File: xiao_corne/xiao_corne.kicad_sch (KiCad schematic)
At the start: 168 parts, among them J1 Conn_01x04_Socket, J10 Conn_01x04_Socket, J2 Conn_01x04_Socket, J3 Conn_01x04_Socket, J4 Conn_01x04_Socket, J5 Conn_01x04_Socket, J6 Conn_01x04_Socket, J7 Conn_01x04_Socket, J8 Conn_01x04_Socket, J9 Conn_01x04_Socket, SW1 SW_Push, SW10 SW_Push, SW11 SW_Push, SW12 SW_Push, SW13 SW_Push, SW14 SW_Push, SW15 SW_Push, SW16 SW_Push, SW17 SW_Push, SW18 SW_Push, SW19 SW_Push, SW2 SW_Push, SW20 SW_Push, SW21 SW_Push, SW22 SW_Push, SW23 SW_Push, SW24 SW_Push, SW25 SW_Push, SW26 SW_Push, SW27 SW_Push, SW28 SW_Push, SW29 SW_Push, SW3 SW_Push, SW30 SW_Push, SW31 SW_Push, SW32 SW_Push, SW33 SW_Push, SW34 SW_Push, SW35 SW_Push, SW36 SW_Push, SW37 SW_Push, SW38 SW_Push, SW39 SW_Push, SW4 SW_Push, SW40 SW_Push, SW41 SW_Push, SW42 SW_Push, SW5 SW_Push, SW6 SW_Push, SW7 SW_Push, SW8 SW_Push, SW9 SW_Push, U1 SN74AHCT125DR, U2 SN74AHCT125DR, U3 XIAO-HALF-HOLE-23P, U4 XIAO-HALF-HOLE-23P, U5 TPS61202DRCR, U6 TPS61202DRCR

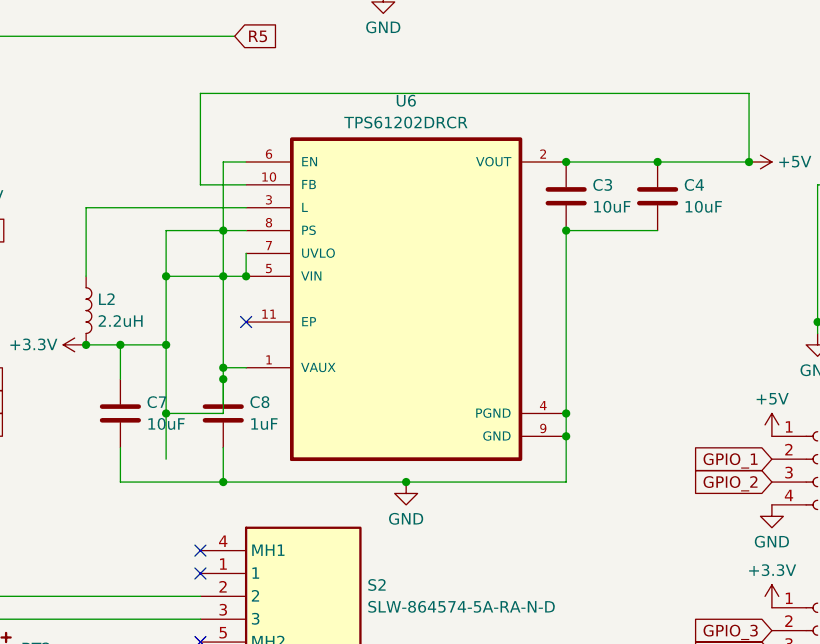
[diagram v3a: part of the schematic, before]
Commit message: Found some issues with the PCB, updated layout
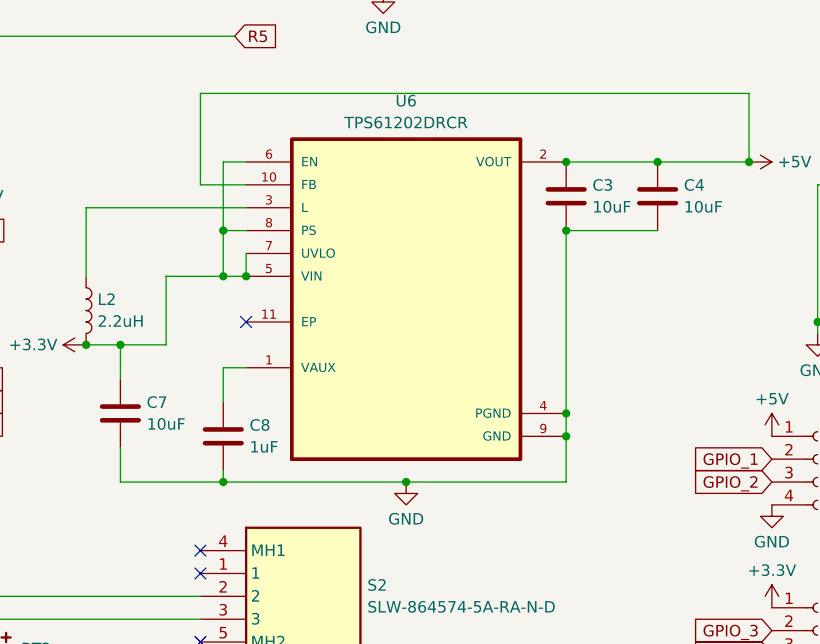
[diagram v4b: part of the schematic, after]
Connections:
- net +3.3V: no longer C8.2, U6.1 (VAUX)
- new net: C8.2, U6.1 (VAUX)
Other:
- moved on the sheet: C8
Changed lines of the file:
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@@
 	)
 	(junction
-		(at 415.29 152.4)
-		(diameter 0)
-		(color 0 0 0 0)
-	)
-	(junction
 		(at 213.36 67.31)
 		(diameter 0)
@@
 	)
 	(junction
-		(at 408.94 148.59)
-		(diameter 0)
-		(color 0 0 0 0)
-	)
-	(junction
 		(at 400.05 38.1)
 		(diameter 0)
@@
 	)
 	(junction
+		(at 453.39 128.27)
+		(diameter 0)
+		(color 0 0 0 0)
+	)
+	(junction
 		(at 116.84 38.1)
 		(diameter 0)
@@
 	)
 	(junction
-		(at 408.94 140.97)
-		(diameter 0)
-		(color 0 0 0 0)
-	)
-	(junction
 		(at 453.39 156.21)
 		(diameter 0)
@@
 	)
 	(junction
-		(at 453.39 128.27)
-		(diameter 0)
-		(color 0 0 0 0)
-	)
-	(junction
 		(at 228.6 82.55)
 		(diameter 0)
@@
 	)
 	(junction
-		(at 408.94 156.21)
-		(diameter 0)
-		(color 0 0 0 0)
-	)
-	(junction
 		(at 400.05 76.2)
 		(diameter 0)
@@
 	)
 	(junction
-		(at 415.29 151.13)
-		(diameter 0)
-		(color 0 0 0 0)
-	)
-	(junction
 		(at 167.64 39.37)
 		(diameter 0)
@@
 	(wire
 		(pts
+			(xy 415.29 162.56) (xy 415.29 163.83)
+		)
+		(stroke
+			(width 0)
+			(type default)
+		)
+	)
+	(wire
+		(pts
 			(xy 133.35 95.25) (xy 116.84 95.25)
 		)
@@
 	(wire
 		(pts
-			(xy 44.45 46.99) (xy 44.45 66.04)
+			(xy 417.83 138.43) (xy 417.83 140.97)
 		)
 		(stroke
@@
 	(wire
 		(pts
-			(xy 259.08 93.98) (xy 243.84 93.98)
+			(xy 44.45 46.99) (xy 44.45 66.04)
 		)
 		(stroke
@@
 	(wire
 		(pts
-			(xy 114.3 162.56) (xy 125.73 162.56)
+			(xy 259.08 93.98) (xy 243.84 93.98)
 		)
 		(stroke
@@
 	(wire
 		(pts
-			(xy 73.66 95.25) (xy 95.25 95.25)
+			(xy 114.3 162.56) (xy 125.73 162.56)
 		)
 		(stroke
@@
 	(wire
 		(pts
-			(xy 463.55 128.27) (xy 453.39 128.27)
+			(xy 73.66 95.25) (xy 95.25 95.25)
 		)
 		(stroke
@@
 	(wire
 		(pts
-			(xy 417.83 138.43) (xy 417.83 140.97)
-		)
-		(stroke
-			(width 0)
-			(type default)
-		)
-	)
-	(wire
-		(pts
 			(xy 173.99 127) (xy 163.83 127)
 		)
@@
 	(wire
 		(pts
-			(xy 408.94 148.59) (xy 408.94 156.21)
-		)
-		(stroke
-			(width 0)
-			(type default)
-		)
-	)
-	(wire
-		(pts
 			(xy 440.69 101.6) (xy 443.23 101.6)
 		)
@@
 	(wire
 		(pts
-			(xy 565.15 74.93) (xy 565.15 83.82)
+			(xy 453.39 128.27) (xy 463.55 128.27)
 		)
 		(stroke
@@
 	(wire
 		(pts
-			(xy 403.86 148.59) (xy 408.94 148.59)
+			(xy 565.15 74.93) (xy 565.15 83.82)
 		)
 		(stroke
@@
 	(wire
 		(pts
-			(xy 412.75 120.65) (xy 473.71 120.65)
+			(xy 403.86 148.59) (xy 408.94 148.59)
 		)
 		(stroke
@@
 	(wire
 		(pts
-			(xy 128.27 134.62) (xy 125.73 134.62)
+			(xy 412.75 120.65) (xy 473.71 120.65)
 		)
 		(stroke
@@
 	(wire
 		(pts
-			(xy 415.29 151.13) (xy 417.83 151.13)
+			(xy 128.27 134.62) (xy 125.73 134.62)
 		)
 		(stroke
@@
 	(wire
 		(pts
-			(xy 73.66 172.72) (xy 73.66 176.53)
+			(xy 415.29 140.97) (xy 408.94 140.97)
 		)
 		(stroke
@@
 	(wire
 		(pts
-			(xy 481.33 82.55) (xy 496.57 82.55)
+			(xy 415.29 151.13) (xy 415.29 154.94)
 		)
 		(stroke
@@
 	(wire
 		(pts
-			(xy 341.63 175.26) (xy 340.36 175.26)
+			(xy 73.66 172.72) (xy 73.66 176.53)
 		)
 		(stroke
@@
 	(wire
 		(pts
-			(xy 557.53 93.98) (xy 542.29 93.98)
+			(xy 481.33 82.55) (xy 496.57 82.55)
 		)
 		(stroke
@@
 	(wire
 		(pts
-			(xy 182.88 67.31) (xy 198.12 67.31)
+			(xy 341.63 175.26) (xy 340.36 175.26)
 		)
 		(stroke
@@
 	(wire
 		(pts
-			(xy 433.07 109.22) (xy 433.07 82.55)
+			(xy 557.53 93.98) (xy 542.29 93.98)
 		)
 		(stroke
@@
 	(wire
 		(pts
-			(xy 389.89 179.07) (xy 412.75 179.07)
+			(xy 182.88 67.31) (xy 198.12 67.31)
 		)
 		(stroke
@@
 	(wire
 		(pts
-			(xy 392.43 66.04) (xy 392.43 85.09)
+			(xy 433.07 109.22) (xy 433.07 82.55)
 		)
 		(stroke
@@
 	(wire
 		(pts
-			(xy 228.6 39.37) (xy 213.36 39.37)
+			(xy 389.89 179.07) (xy 412.75 179.07)
 		)
 		(stroke
@@
 	(wire
 		(pts
-			(xy 119.38 147.32) (xy 119.38 139.7)
+			(xy 392.43 66.04) (xy 392.43 85.09)
 		)
 		(stroke
@@
 	(wire
 		(pts
-			(xy 415.29 135.89) (xy 408.94 135.89)
+			(xy 228.6 39.37) (xy 213.36 39.37)
 		)
 		(stroke
@@
 	(wire
 		(pts
-			(xy 243.84 39.37) (xy 228.6 39.37)
+			(xy 119.38 147.32) (xy 119.38 139.7)
 		)
 		(stroke
@@
 	(wire
 		(pts
-			(xy 378.46 57.15) (xy 400.05 57.15)
+			(xy 243.84 39.37) (xy 228.6 39.37)
 		)
 		(stroke
@@
 	(wire
 		(pts
-			(xy 434.34 46.99) (xy 443.23 46.99)
+			(xy 378.46 57.15) (xy 400.05 57.15)
 		)
 		(stroke
@@
 	(wire
 		(pts
-			(xy 335.28 57.15) (xy 356.87 57.15)
+			(xy 434.34 46.99) (xy 443.23 46.99)
 		)
 		(stroke
@@
 	(wire
 		(pts
-			(xy 408.94 156.21) (xy 408.94 161.29)
+			(xy 335.28 57.15) (xy 356.87 57.15)
 		)
 		(stroke
@@
 	(wire
 		(pts
-			(xy 415.29 140.97) (xy 415.29 151.13)
-		)
-		(stroke
-			(width 0)
-			(type default)
-		)
-	)
-	(wire
-		(pts
 			(xy 198.12 54.61) (xy 182.88 54.61)
 		)
@@
 	(wire
 		(pts
-			(xy 415.29 152.4) (xy 415.29 156.21)
-		)
-		(stroke
-			(width 0)
-			(type default)
-		)
-	)
-	(wire
-		(pts
 			(xy 274.32 54.61) (xy 259.08 54.61)
 		)
@@
 	(wire
 		(pts
+			(xy 415.29 151.13) (xy 417.83 151.13)
+		)
+		(stroke
+			(width 0)
+			(type default)
+		)
+	)
+	(wire
+		(pts
 			(xy 450.85 54.61) (xy 433.07 54.61)
 		)
@@
 	(wire
 		(pts
-			(xy 415.29 160.02) (xy 415.29 163.83)
-		)
-		(stroke
-			(width 0)
-			(type default)
-		)
-	)
-	(wire
-		(pts
 			(xy 511.81 54.61) (xy 496.57 54.61)
 		)
@@
 	(wire
 		(pts
-			(xy 415.29 140.97) (xy 408.94 140.97)
-		)
-		(stroke
-			(width 0)
-			(type default)
-		)
-	)
-	(wire
-		(pts
 			(xy 144.78 162.56) (xy 163.83 162.56)
 		)
@@
 	(wire
 		(pts
-			(xy 415.29 151.13) (xy 415.29 152.4)
-		)
-		(stroke
-			(width 0)
-			(type default)
-		)
-	)
-	(wire
-		(pts
 			(xy 259.08 67.31) (xy 274.32 67.31)
 		)
@@
 	(wire
 		(pts
-			(xy 415.29 156.21) (xy 408.94 156.21)
-		)
-		(stroke
-			(width 0)
-			(type default)
-		)
-	)
-	(wire
-		(pts
 			(xy 417.83 135.89) (xy 415.29 135.89)
 		)
@@
 	(wire
 		(pts
-			(xy 408.94 135.89) (xy 408.94 140.97)
-		)
-		(stroke
-			(width 0)
-			(type default)
-		)
-	)
-	(wire
-		(pts
 			(xy 408.94 140.97) (xy 408.94 148.59)
 		)
@@
 	(symbol
 		(lib_id "Device:C")
-		(at 415.29 156.21 180)
+		(at 415.29 158.75 180)
 		(unit 1)
 		(exclude_from_sim no)
@@
 		(fields_autoplaced yes)
 		(property "Reference" "C8"
-			(at 418.211 154.9978 0)
+			(at 418.211 157.5378 0)
 			(effects
 				(font
@@
 		)
 		(property "Value" "1uF"
-			(at 418.211 157.4221 0)
+			(at 418.211 159.9621 0)
 			(effects
 				(font
@@
 		)
 		(property "Footprint" "Capacitor_SMD:C_0603_1608Metric"
-			(at 414.3248 152.4 0)
+			(at 414.3248 154.94 0)
 			(effects
 				(font
@@
 		)
 		(property "Datasheet" "~"
-			(at 415.29 156.21 0)
+			(at 415.29 158.75 0)
 			(effects
 				(font
@@
 		)
 		(property "Description" "Unpolarized capacitor"
-			(at 415.29 156.21 0)
+			(at 415.29 158.75 0)
 			(effects
 				(font

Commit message: WIP large upgrade to keyboard design
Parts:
- removed BT2: Battery, ScottoKeebs_Scotto:Battery, symbol Device:Battery
- removed C10: 100nF, Capacitor_SMD:C_0805_2012Metric, symbol Device:C
- removed C3, C4, C7: 10uF, Capacitor_SMD:C_0805_2012Metric, symbol Device:C
- removed C8: 1uF, Capacitor_SMD:C_0603_1608Metric, symbol Device:C
- removed D10, D24, D25, D26, D27, D28, D42, D43, D44, D45, D46, D6, D68, D69, D7, D70, D71, D72, D8, D9, D90: D, ScottoKeebs_Components:Diode_SOD-123, symbol Device:D
- removed D29, D30, D31, D32, D33, D34, D35, D36, D55, D56, D57, D58, D59, D60, D61, D62, D81, D82, D83, D84, D85, D86, D87, D88: LED_SK6812MINI, ScottoKeebs_Components:LED_SK6812MINI, symbol ScottoKeebs:LED_SK6812MINI
- removed J1, J10, J2, J3, J4, J5, J7, J8, J9: Conn_01x04_Socket, Connector_PinHeader_2.54mm:PinHeader_1x04_P2.54mm_Vertical, symbol Connector:Conn_01x04_Socket
- removed L2: 2.2uH, Inductor_SMD:L_0805_2012Metric, symbol Device:L
- removed S2: SLW-864574-5A-RA-N-D, KiCad:SLW8645745ARAND, symbol SLW-864574-5A-RA-N-D:SLW-864574-5A-RA-N-D
- removed SW10, SW16, SW17, SW18, SW19, SW20, SW26, SW27, SW28, SW29, SW30, SW36, SW37, SW38, SW39, SW40, SW42, SW6, SW7, SW8, SW9: SW_Push, ScottoKeebs_Hotswap:Hotswap_Choc_V1V2_1.00u, symbol Switch:SW_Push
- removed U2: SN74AHCT125DR, footprints_sn7:D14, symbol 2025-03-05_20-42-17:SN74AHCT125DR
- removed U3, U4: XIAO-HALF-HOLE-23P, xiao ESP32S3 Plus_PCB:MOUDLE23P-SMD-2.54-21X17.8MM.kicad_mod.kicad_sym, symbol MOUDLE-SEEEDUINO-XIAO-ESP32S3-Plus:Module/XIAO-HALF-HOLE-23P
- removed U6: TPS61202DRCR, TPS61202DRCR:VREG_V62_16624-01YE, symbol TPS61202DRCR:TPS61202DRCR
- added J1: USB4110GFA, USB4110GFA:GCT_USB4110GFA, symbol USB4110GFA:USB4110GFA
- added R5, R6: 5.1k, symbol Device:R
- added U2: ESP32-S3-WROOM-1, PCM_Espressif:ESP32-S3-WROOM-1, symbol PCM_Espressif:ESP32-S3-WROOM-1
- added U3: TPS61201DRCT, TPS61201DRCT:VREG_V62_16624-01YE, symbol TPS61201DRCT:TPS61201DRCT
- R2, R4: value 100k -> R; footprint Resistor_SMD:R_0805_2012Metric -> (none)
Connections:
- net GND: now also J1.A1/B12 (GND), J1.B1/A12 (GND__1), J1.S1 (GND__2), J1.S2 (GND__3), J1.S3 (GND__4), J1.S4 (GND__5), R5.2, R6.2; no longer R2.2
- net at R4.2: now also J1.A7 (DN1), J1.B7 (DN2)
- net at R4.1: no longer R2.1
- new net: J1.B5 (CC2), R5.1
- new net: J1.A5 (CC1), R6.1
- new net: J1.A6 (DP1), J1.B6 (DP2), R2.2
- new net: U2.1 (GND), U2.40 (GND), U2.41 (GND)
- new net VUSB: J1.A4/B9 (VBUS), J1.B4/A9 (VBUS__1)
- no-connect marks 46 -> 19
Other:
- note added: "3.3 ish power level"
- note added: "3.3v regulator"
- note added: "5v regulator"
- note added: "Battery charging"
- note added: "Battery monitor"
- note added: "Keyswitch array"
- note added: "LED array"
- note added: "LED logic level converter"
- note added: "Other External connections"
- note added: "Ref https://github.com/microbotsio/CodeCell/blob/main/hardware/CodeCell%20C3/CodeCell%20Schematics.pdf"
- note added: "USB / MCU"
- moved on the sheet: C1, C2, C5, C6, C9, D16, D17, D18, D19, D20, D21, D22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

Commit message: Finished sketch of schematic
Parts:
- removed C1, C2, C5: 10uF, Capacitor_SMD:C_0805_2012Metric, symbol Device:C
- removed C6: 1uF, Capacitor_SMD:C_0603_1608Metric, symbol Device:C
- removed D1, D11, D12, D13, D14, D15, D2, D3, D37, D38, D39, D4, D40, D41, D5, D63, D64, D65, D66, D67, D89: D, ScottoKeebs_Components:Diode_SOD-123, symbol Device:D
- removed L1: 2.2uH, Inductor_SMD:L_0805_2012Metric, symbol Device:L
- removed U5: TPS61202DRCR, TPS61202DRCR:VREG_V62_16624-01YE, symbol TPS61202DRCR:TPS61202DRCR
- added C10, C12, C13: 10uF, Capacitor_SMD:C_0805_2012Metric, symbol Device:C
- added C11: 1uF, Capacitor_SMD:C_0603_1608Metric, symbol Device:C
- added C14, C15, C16: 4.7u, symbol Device:C
- added C3: 1u, symbol Device:C
- added C4: 22u, symbol Device:C
- added C7: 0.1u, symbol Device:C
- added C8: C, symbol Device:C
- added H1, H2, H3: MountingHole_Pad, symbol Mechanical:MountingHole_Pad
- added L2: 2.2uH, Inductor_SMD:L_0805_2012Metric, symbol Device:L
- added R10, R7, R8, R9: 10k, symbol Device:R
- added SW6: SW_Push, symbol Switch:SW_Push
- added U4: BQ24232RGTR, RGT0016C, symbol 2026-02-16_20-39-13:BQ24232RGTR
- R2, R4: value R -> 22
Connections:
- net +5V L is gone; now on net +4.4V L: D16.1 (VDD), D17.1 (VDD), D18.1 (VDD), D19.1 (VDD), D20.1 (VDD), D21.1 (VDD), D22.1 (VDD), D23.1 (VDD), D47.1 (VDD), D48.1 (VDD), D49.1 (VDD), D50.1 (VDD), D51.1 (VDD), D52.1 (VDD), D53.1 (VDD), D54.1 (VDD), D73.1 (VDD), D74.1 (VDD), D75.1 (VDD), D76.1 (VDD), D77.1 (VDD), D78.1 (VDD), D79.1 (VDD), D80.1 (VDD), U1.14 (VCC)
- net +3.3V L: now also SW1.1, SW11.1, SW12.1, SW13.1, SW14.1, SW15.1, SW2.1, SW21.1, SW22.1, SW23.1, SW24.1, SW25.1, SW3.1, SW31.1, SW32.1, SW33.1, SW34.1, SW35.1, SW4.1, SW41.1, SW5.1, U2.2 (3V3), U3.10 (FB), U3.2 (VOUT), C12.2, C13.2, C4.2, C7.2, R7.1, R8.2
- net +5V L USB: no longer J6.1 (Pin_1)
- net GND: now also U2.1 (GND), U2.40 (GND), U2.41 (GND), C14.2, C15.2, C16.2, C3.1, C4.1, C7.1, C8.2, H1.1, H2.1, H3.1, R10.2, R9.1, SW6.1, U4.17 (EP), U4.4 (CE_N), U4.5 (EN2), U4.8 (VSS)
- net GND L: now also R1.1, U3.4 (PGND), U3.9 (GND), C10.1, C11.1, C12.1, C13.1; no longer R1.2
- net VUSB: now also J6.1 (Pin_1), C16.1, U4.13 (IN)
- net at R4.1: now also U2.13 (GPIO19/U1RTS/ADC2_CH8/CLK_OUT2/USB_D-)
- net at U3.1 (VAUX): now also C11.2
- net at U3.3 (L): now also L2.1
- net +4.4V L: now reaches U3.5 (VIN)
- net +4.4V L: now also U3.6 (EN), U3.7 (UVLO), U3.8 (PS), C10.2, C15.1, L2.2, U4.10 (OUT), U4.11 (OUT), U4.6 (EN1)
- net BAT/2 MON: now reaches C9.2, R3.1
- net BAT/2 MON: now also R1.2, U2.39 (GPIO1/TOUCH1/ADC1_CH0); no longer R1.1
- net at U2.14 (GPIO20/U1CTS/ADC2_CH9/CLK_OUT1/USB_D+): now also R2.1
- net at U2.27 (GPIO0/BOOT): now also C8.1, R8.1, SW6.2
- net at U2.3 (EN): now also C3.2, R7.2
- net VBAT: now reaches R3.2, S1.2
- net VBAT: now also C14.1, U4.2 (BAT), U4.3 (BAT)
- removed net R1 L: SW1.2, SW2.2, SW3.2, SW4.2, SW5.2
- removed net R2 L: SW11.2, SW12.2, SW13.2, SW14.2, SW15.2
- removed net R3 L: SW21.2, SW22.2, SW23.2, SW24.2, SW25.2
- removed net R4 L: SW31.2, SW32.2, SW33.2, SW34.2, SW35.2
- net R5 L renamed KS_L21
- new net: R9.2, U4.1 (TS)
- new net: R10.1, U4.16 (ISET)
- new net KS_L1: SW1.2
- new net KS_L10: SW15.2
- new net KS_L11: SW21.2
- new net KS_L12: SW22.2
- new net KS_L13: SW23.2
- new net KS_L14: SW24.2
- new net KS_L15: SW25.2
- new net KS_L16: SW31.2
- new net KS_L17: SW32.2
- new net KS_L18: SW33.2
- new net KS_L19: SW34.2
- new net KS_L2: SW2.2
- new net KS_L20: SW35.2
- new net KS_L3: SW3.2
- new net KS_L4: SW4.2
- new net KS_L5: SW5.2
- new net KS_L6: SW11.2
- new net KS_L7: SW12.2
- new net KS_L8: SW13.2
- new net KS_L9: SW14.2
- new net pgood: U4.7 (PGOOD_N)
- no-connect marks 19 -> 22
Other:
- note added: "Battery monitor / switch"
- note added: "Boot Button"
- note added: "Boot delay"
- note added: "Power filtering"
- note added: "USB C"
- note removed: "3.3 ish power level"
- note removed: "5v regulator"
- note removed: "Battery monitor"
- moved on the sheet: BT1, C9, J1, J6, R1, R2, R3, R4, R5, R6, S1, U1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

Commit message: starting layout for left side
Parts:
- removed D78, D79, D80: LED_SK6812MINI, ScottoKeebs_Components:LED_SK6812MINI, symbol ScottoKeebs:LED_SK6812MINI
- added D1, D2: ESD321DPYR, ESD321DPYR:TVS_ESD321DPYR, symbol ESD321DPYR:ESD321DPYR
- BT1: footprint ScottoKeebs_Scotto:Battery -> Connector_PinHeader_2.00mm:PinHeader_1x02_P2.00mm_Vertical
- C11: value 1uF -> 0.1uF; footprint Capacitor_SMD:C_0603_1608Metric -> Capacitor_SMD:C_0805_2012Metric
- C14, C15, C16, C3, C4, C7: footprint (none) -> Capacitor_SMD:C_0805_2012Metric
- C8: value C -> 100nF; footprint (none) -> Capacitor_SMD:C_0805_2012Metric
- D16, D17, D18, D19, D20, D21, D22, D23, D47, D48, D49, D50, D51, D52, D53, D54, D73, D74, D75, D76, D77: footprint ScottoKeebs_Components:LED_SK6812MINI -> footprints:LED_SK6812MINI
- H1, H2, H3: footprint (none) -> MountingHole:MountingHole_3.2mm_M3_ISO14580
- J1: footprint USB4110GFA:GCT_USB4110GFA -> USB4110_GF_A:GCT_USB4110GFA
- R10, R2, R4, R5, R6, R7, R8, R9: footprint (none) -> Resistor_SMD:R_0805_2012Metric
- S1: footprint KiCad:SLW8645745ARAND -> SLW_864574_5A_RA_N_D:SW_SLW-864574-5A-RA-N-D
- SW1, SW11, SW12, SW13, SW14, SW15, SW2, SW21, SW22, SW23, SW24, SW25, SW3, SW31, SW32, SW33, SW34, SW35, SW4, SW41, SW5: footprint ScottoKeebs_Hotswap:Hotswap_Choc_V1V2_1.00u -> footprints:Hotswap_Choc_V1V2
- SW6: footprint (none) -> footprints:MJTP1117
- U1: footprint footprints_sn7:D14 -> footprints-sn7:D14
- U4: footprint RGT0016C -> BQ24232RGTR:RGT0016C
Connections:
- net BAT/2 MON is gone; now on net BAT/2 MON L: C9.2, R1.2, R3.1, U2.39 (GPIO1/TOUCH1/ADC1_CH0)
- net pgood is gone; now on net pgood L: U4.7 (PGOOD_N)
- net GND: no longer C14.2, C15.2, C16.2, C3.1, C4.1, C7.1, C8.2, H1.1, H2.1, H3.1, J1.A1/B12 (GND), J1.B1/A12 (GND__1), J1.S1 (GND__2), J1.S2 (GND__3), J1.S3 (GND__4), J1.S4 (GND__5), R10.2, R5.2, R6.2, R9.1, SW6.1, U4.17 (EP), U4.5 (EN2), U4.8 (VSS)
- net GND L: now also C14.2, C15.2, C16.2, C3.1, C4.1, C7.1, C8.2, H1.1, H2.1, H3.1, J1.A1/B12 (GND), J1.B1/A12 (GND__1), J1.S1 (GND__2), J1.S2 (GND__3), J1.S3 (GND__4), J1.S4 (GND__5), R10.2, R5.2, R6.2, R9.1, SW6.1, U4.17 (EP), U4.5 (EN2), U4.8 (VSS), D1.2, D2.2
- net KS_L1: now also U2.38 (GPIO2/TOUCH2/ADC1_CH1)
- net KS_L10: now also U2.19 (GPIO11/TOUCH11/ADC2_CH0/FSPID/FSPIIO5/SUBSPID)
- net KS_L11: now also U2.20 (GPIO12/TOUCH12/ADC2_CH1/FSPICLK/FSPIIO6/SUBSPICLK)
- net KS_L12: now also U2.21 (GPIO13/TOUCH13/ADC2_CH2/FSPIQ/FSPIIO7/SUBSPIQ)
- net KS_L13: now also U2.22 (GPIO14/TOUCH14/ADC2_CH3/FSPIWP/FSPIDQS/SUBSPIWP)
- net KS_L14: now also U2.10 (GPIO17/U1TXD/ADC2_CH6)
- net KS_L15: now also U2.11 (GPIO18/U1RXD/ADC2_CH7/CLK_OUT3)
- net KS_L16: now also U2.23 (GPIO21)
- net KS_L17: now also U2.31 (GPIO38/FSPIWP/SUBSPIWP)
- net KS_L18: now also U2.26 (GPIO45)
- net KS_L19: now also U2.16 (GPIO46)
- net KS_L2: now also U2.15 (GPIO3/TOUCH3/ADC1_CH2)
- net KS_L20: now also U2.24 (GPIO47/SPICLK_P/SUBSPICLK_P_DIFF)
- net KS_L21: now also U2.25 (GPIO48/SPICLK_N/SUBSPICLK_N_DIFF)
- net KS_L3: now also U2.4 (GPIO4/TOUCH4/ADC1_CH3)
- net KS_L4: now also U2.5 (GPIO5/TOUCH5/ADC1_CH4)
- net KS_L5: now also U2.6 (GPIO6/TOUCH6/ADC1_CH5)
- net KS_L6: now also U2.7 (GPIO7/TOUCH7/ADC1_CH6)
- net KS_L7: now also U2.12 (GPIO8/TOUCH8/ADC1_CH7/SUBSPICS1)
- net KS_L8: now also U2.17 (GPIO9/TOUCH9/ADC1_CH8/FSPIHD/SUBSPIHD)
- net KS_L9: now also U2.18 (GPIO10/TOUCH10/ADC1_CH9/FSPICS0/FSPIIO4/SUBSPICS0)
- net LED_3v L: now also U2.30 (SPIDQS/GPIO37/FSPIQ/SUBSPIQ)
- net at J1.A7 (DN1), J1.B7 (DN2), R4.2: now also D1.1
- net at J1.A6 (DP1), J1.B6 (DP2), R2.2: now also D2.1
- net pgood L: now reaches U2.28 (SPIIO6/GPIO35/FSPID/SUBSPID)
- net BAT/2 MON L: now reaches U2.29 (SPIIO7/GPIO36/FSPICLK/SUBSPICLK)
- net VBAT renamed VBAT L
- net VUSB renamed VUSB L
- no-connect marks 22 -> 30
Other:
- moved on the sheet: SW1, SW11, SW12, SW13, SW14, SW15, SW2, SW21, SW22, SW23, SW24, SW25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

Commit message: almost done routing left half!
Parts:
- H1, H2, H3: footprint MountingHole:MountingHole_3.2mm_M3_ISO14580 -> MountingHole:MountingHole_2.2mm_M2_ISO14580_Pad_TopBottom
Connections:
- net d-: now reaches R4.1, U2.13 (GPIO19/U1RTS/ADC2_CH8/CLK_OUT2/USB_D-)
- net d+: now reaches R2.1, U2.14 (GPIO20/U1CTS/ADC2_CH9/CLK_OUT1/USB_D+)
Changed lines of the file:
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@@
 		)
 	)
+	(global_label "d-"
+		(shape input)
+		(at 293.37 264.16 90)
+		(fields_autoplaced yes)
+		(effects
+			(font
+				(size 1.27 1.27)
+			)
+			(justify left)
+		)
+		(property "Intersheetrefs" "${INTERSHEET_REFS}"
+			(at 293.37 258.4534 90)
+			(effects
+				(font
+					(size 1.27 1.27)
+				)
+				(justify left)
+				(hide yes)
+			)
+		)
+	)
 	(global_label "KS_L3"
 		(shape input)
@@
 		)
 	)
+	(global_label "d+"
+		(shape input)
+		(at 288.29 261.62 90)
+		(fields_autoplaced yes)
+		(effects
+			(font
+				(size 1.27 1.27)
+			)
+			(justify left)
+		)
+		(property "Intersheetrefs" "${INTERSHEET_REFS}"
+			(at 288.29 255.9134 90)
+			(effects
+				(font
+					(size 1.27 1.27)
+				)
+				(justify left)
+				(hide yes)
+			)
+		)
+	)
 	(global_label "KS_L8"
 		(shape input)
@@
 			)
 		)
-		(property "Footprint" "MountingHole:MountingHole_3.2mm_M3_ISO14580"
+		(property "Footprint" "MountingHole:MountingHole_2.2mm_M2_ISO14580_Pad_TopBottom"
 			(at 344.17 167.64 0)
 			(effects
@@
 			)
 		)
-		(property "Footprint" "MountingHole:MountingHole_3.2mm_M3_ISO14580"
+		(property "Footprint" "MountingHole:MountingHole_2.2mm_M2_ISO14580_Pad_TopBottom"
 			(at 316.23 166.37 0)
 			(effects
@@
 			)
 		)
-		(property "Footprint" "MountingHole:MountingHole_3.2mm_M3_ISO14580"
+		(property "Footprint" "MountingHole:MountingHole_2.2mm_M2_ISO14580_Pad_TopBottom"
 			(at 290.83 166.37 0)
 			(effects
